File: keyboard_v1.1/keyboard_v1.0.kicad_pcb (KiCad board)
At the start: 2 copper layers, 100 x 100 mm, 138 parts, among them M3 MountingHole_3.2mm_M3, P1 USB_C_Plug, Q1 AO3400A, Q2 AO3400A, Q3 AO3400A, Q4 AO3400A, SW1 Cherry_MX_1u, SW10 Cherry_MX_1u, SW11 Cherry_MX_1u, SW12 Cherry_MX_1u, SW13 MTS-102, SW14 SW_DIP_x01, SW15 SW_DIP_x01, SW16 SW_DIP_x01, SW17 SW_DIP_x01, SW2 Cherry_MX_1u, SW3 Cherry_MX_1u, SW4 Cherry_MX_1u, SW5 Cherry_MX_1u, SW6 Cherry_MX_1u, SW7 Cherry_MX_1u, SW8 Cherry_MX_1u, SW9 Cherry_MX_1u, U1 max1737eei+T, U2 max1771esa+T, U3 max1771esa+T

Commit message: PCB layout done - 2022.07.25.
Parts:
- removed C25, C32, C33, C34, C35, C36, C37, C41, C46: 0.1uF, Capacitor_SMD:C_0805_2012Metric_Pad1.18x1.45mm_HandSolder
- removed C26: 47nF, Capacitor_SMD:C_0805_2012Metric_Pad1.18x1.45mm_HandSolder
- removed C27, C29, C30: 1nF, Capacitor_SMD:C_0805_2012Metric_Pad1.18x1.45mm_HandSolder
- removed C28: 4.7u, Capacitor_SMD:C_0805_2012Metric_Pad1.18x1.45mm_HandSolder
- removed C38, C39: 22pF, Capacitor_SMD:C_0805_2012Metric_Pad1.18x1.45mm_HandSolder
- removed C40: 68uF, Capacitor_THT:CP_Radial_D6.3mm_P2.50mm
- removed C42, C47: 2.2uF, Capacitor_SMD:C_0805_2012Metric_Pad1.18x1.45mm_HandSolder
- removed C43, C48: 47pF, Capacitor_SMD:C_0805_2012Metric_Pad1.18x1.45mm_HandSolder
- removed C44, C49: 47uF, Capacitor_THT:CP_Radial_D4.0mm_P1.50mm
- removed C45, C50: 22uF, Capacitor_SMD:C_0805_2012Metric_Pad1.18x1.45mm_HandSolder
- removed D35, D39: US1M, Diode_SMD:D_SMA
- removed D38: LED, LED_SMD:LED_0603_1608Metric_Pad1.05x0.95mm_HandSolder
- removed D40, D41, D42, D43: 1N5819, Diode_THT:D_DO-41_SOD81_P10.16mm_Horizontal
- removed L4, L5: 20uH, inductors:inductors
- removed the M3 at (135.0, 125.0)
- removed the M3 at (45.0, 125.0)
- removed the M3 at (135.0, 35.0)
- removed the M3 at (45.0, 35.0)
- removed Q1 (x2), Q2 (x2), Q3, Q4: AO3400A, Package_TO_SOT_SMD:SOT-23
- removed R30: 200K, Resistor_SMD:R_0805_2012Metric_Pad1.20x1.40mm_HandSolder
- removed R31: 470K, Resistor_SMD:R_0805_2012Metric_Pad1.20x1.40mm_HandSolder
- removed R32, R35: 0.1, Resistor_SMD:R_0805_2012Metric_Pad1.20x1.40mm_HandSolder
- removed R33: 100K, Resistor_SMD:R_0805_2012Metric_Pad1.20x1.40mm_HandSolder
- removed R34: 20K, Resistor_SMD:R_0805_2012Metric_Pad1.20x1.40mm_HandSolder
- removed SW14, SW15, SW16, SW17: SW_DIP_x01, Connector_PinHeader_2.54mm:PinHeader_1x02_P2.54mm_Vertical
- removed TH1: Thermistor_NTC, Capacitor_THT:C_Disc_D5.0mm_W2.5mm_P5.00mm
- removed U2, U3: max1771esa+T, max1771:max1771esa&plus_T
- added C13: 10uF, Capacitor_SMD:C_0805_2012Metric_Pad1.18x1.45mm_HandSolder, F.Cu at (80.8, 50.3)
- added C15: 22uF, Capacitor_SMD:C_0805_2012Metric_Pad1.18x1.45mm_HandSolder, F.Cu at (75.9, 54.2)
- added C16: 1uF, Capacitor_SMD:C_0805_2012Metric_Pad1.18x1.45mm_HandSolder, F.Cu at (77.9, 54.2)
- added C17: 22uF, Capacitor_SMD:C_0805_2012Metric_Pad1.18x1.45mm_HandSolder, F.Cu at (104.8, 53.2)
- added C18: 2.2uF, Capacitor_SMD:C_0805_2012Metric_Pad1.18x1.45mm_HandSolder, F.Cu at (112.8, 51.4)
- added C9: 4.7uF, Capacitor_SMD:C_0805_2012Metric_Pad1.18x1.45mm_HandSolder, F.Cu at (97.0, 32.9)
- added D14: FUXINSEMI DSK34 (SOD-123), Diode_SMD:D_SOD-123, F.Cu at (114.1, 47.2)
- added IC1: LN4056-ESOP8, SamacSys_Parts:SOIC127P600X175-9N, F.Cu at (98.8, 36.7)
- added JP1: Jumper_3_Bridged12, Connector_PinHeader_2.54mm:PinHeader_1x03_P2.54mm_Horizontal, F.Cu at (135.1, 71.7)
- added JP2: Jumper_3_Bridged12, Connector_PinHeader_2.54mm:PinHeader_1x03_P2.54mm_Horizontal, F.Cu at (135.1, 80.3)
- added JP3: Jumper_3_Bridged12, Connector_PinHeader_2.54mm:PinHeader_1x03_P2.54mm_Horizontal, F.Cu at (135.1, 97.8)
- added JP4: Jumper_3_Bridged12, Connector_PinHeader_2.54mm:PinHeader_1x03_P2.54mm_Horizontal, F.Cu at (135.2, 89.0)
- added M3: MountingHole_3.2mm_M3, MountingHole:MountingHole_3.2mm_M3, F.Cu at (135.4, 125.5)
- added M3: MountingHole_3.2mm_M3, MountingHole:MountingHole_3.2mm_M3, F.Cu at (135.9, 33.9)
- added M3: MountingHole_3.2mm_M3, MountingHole:MountingHole_3.2mm_M3, F.Cu at (44.3, 125.4)
- added M3: MountingHole_3.2mm_M3, MountingHole:MountingHole_3.2mm_M3, F.Cu at (44.6, 34.6)
- added PS1: HX3608, SamacSys_Parts:SOT95P280X125-6N, F.Cu at (81.0, 53.2)
- added R14: 10k, Resistor_SMD:R_0805_2012Metric_Pad1.20x1.40mm_HandSolder, F.Cu at (103.8, 39.6)
- added R15: 22k, Resistor_SMD:R_0805_2012Metric_Pad1.20x1.40mm_HandSolder, F.Cu at (71.5, 54.1)
- added R16: 3k, Resistor_SMD:R_0805_2012Metric_Pad1.20x1.40mm_HandSolder, F.Cu at (71.5, 57.8)
- added R17: 100K, Resistor_SMD:R_0805_2012Metric_Pad1.20x1.40mm_HandSolder, F.Cu at (105.8, 50.4)
- added R18: 9.1k, Resistor_SMD:R_0805_2012Metric_Pad1.20x1.40mm_HandSolder, F.Cu at (109.9, 46.7)
- added R19: 5.6k, Resistor_SMD:R_0805_2012Metric_Pad1.20x1.40mm_HandSolder, F.Cu at (105.1, 47.5)
- added TP2: TestPoint, TestPoint:TestPoint_Keystone_5010-5014_Multipurpose, F.Cu at (109.6, 39.4)
- BT1: footprint Connector_PinSocket_2.54mm:PinSocket_1x02_P2.54mm_Vertical -> Connector_PinSocket_2.54mm:PinSocket_1x02_P2.54mm_Horizontal
- C22: value 4.7u -> 2.2nF
- C23: value 47nF -> 10uF
- C24: value 0.1uF -> ?uF
- C31: value 0.1uF -> 4.7uF
- D13: value US1M -> FUXINSEMI DSK34 (SOD-123); footprint Diode_SMD:D_SMA -> Diode_SMD:D_SOD-123
- D36: value LED -> GREEN LED; footprint LED_SMD:LED_0603_1608Metric_Pad1.05x0.95mm_HandSolder -> LED_SMD:LED_0805_2012Metric_Pad1.15x1.40mm_HandSolder
- D37: value LED -> RED LED; footprint LED_SMD:LED_0603_1608Metric_Pad1.05x0.95mm_HandSolder -> LED_SMD:LED_0805_2012Metric_Pad1.15x1.40mm_HandSolder
- L1: value 22uH -> 3.3uH; footprint inductors:inductors -> inductors:inductor_koherelec
- L2, L3: value 20uH -> 6.8uH; footprint inductors:inductors -> inductors:inductor_koherelec
- R1, R2, R3: moved to F.Cu
- R10: value 1k -> 3k
- R12: value 0.1prec -> 10k; footprint Resistor_SMD:R_2512_6332Metric_Pad1.40x3.35mm_HandSolder -> Resistor_SMD:R_0805_2012Metric_Pad1.20x1.40mm_HandSolder
- R13: value 0.18prec -> 10k; footprint Resistor_THT:R_Axial_DIN0309_L9.0mm_D3.2mm_P25.40mm_Horizontal -> Resistor_SMD:R_0805_2012Metric_Pad1.20x1.40mm_HandSolder
- R9: value 1k -> 10K
- SW13: value MTS-102 -> SW_DPDT; footprint Switch_ApemInc:Apem_Inc.-25336NA-MFG -> Connector_PinHeader_2.54mm:PinHeader_1x03_P2.54mm_Horizontal
- U1: value max1737eei+T -> LMR62421XMF; footprint max1737:max1737eei&plus_T -> Package_TO_SOT_SMD:SOT-23-5
- moved C19 98.9 mm to (138.0, 39.4), turned to 0 degrees
- moved C20 98.4 mm to (138.0, 41.4), turned to 0 degrees
- moved C21 92.6 mm to (135.0, 40.6), turned to 90 degrees
- moved R5 89.4 mm to (131.6, 37.3), turned to -90 degrees
- moved R3 88.3 mm to (130.4, 111.3), turned to -90 degrees
- moved ESP32 87.0 mm to (133.4, 53.5), turned to -90 degrees
- moved R8 85.2 mm to (132.0, 103.9), turned to 90 degrees
- moved R2 83.9 mm to (128.5, 91.4), turned to -90 degrees
- moved R7 75.7 mm to (132.3, 86.4), turned to 90 degrees
- moved C12 74.5 mm to (52.0, 119.9), turned to 180 degrees
- moved C11 72.7 mm to (53.9, 79.7), turned to 180 degrees
- moved R9 72.3 mm to (132.3, 95.1)
- moved R6 70.1 mm to (132.3, 77.7), turned to 90 degrees
- moved C14 67.7 mm to (59.0, 108.7), turned to 0 degrees
- moved P1 67.3 mm to (122.8, 35.7), turned to 0 degrees
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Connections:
- C22 pad 1: Net-(C22-Pad1) -> 3.3V_OUT
- C22 pad 2: GND -> Net-(C22-Pad2)
- C23 pad 1: Net-(C23-Pad1) -> 3.3V_OUT
- C24 pad 1: Net-(C24-Pad1) -> 3.3V_OUT
- C31 pad 1: Net-(C31-Pad1) -> USB_Input_supply
- D13 pad 1: Net-(C36-Pad1) -> 5V_OUT
- D13 pad 2: USB_Input_supply -> Net-(D13-Pad2)
- D37 pad 2: Net-(D37-Pad2) -> Net-(D36-Pad2)
- ESP32 pad 4: 1st_Column -> 4th_Column
- ESP32 pad 5: 2nd_Column -> 3rd_Column
- ESP32 pad 6: 3rd_Column -> 2nd_Column
- ESP32 pad 7: 4th_Column -> 1st_Column
- L1 pad 1: Net-(C33-Pad2) -> SYSTEM_LOAD
- L1 pad 2: Net-(C34-Pad1) -> Net-(D13-Pad2)
- L2 pad 2: Net-(C44-Pad1) -> Net-(C18-Pad1)
- R10 pad 1: Net-(C31-Pad1) -> USB_Input_supply
- R10 pad 2: Net-(D37-Pad2) -> Net-(D36-Pad2)
- R11 pad 1: Net-(C31-Pad1) -> Net-(IC1-Pad2)
- R11 pad 2: Net-(D36-Pad2) -> GND
- R12 pad 1: Net-(C36-Pad1) -> USB_Input_supply
- R12 pad 2: SYSTEM_LOAD -> Net-(IC1-Pad8)
- R13 pad 1: Net-(C34-Pad1) -> USB_Input_supply
- R13 pad 2: Net-(C32-Pad1) -> /battery_charger/TEMP
- R6 pad 1: Net-(C27-Pad1) -> GND
- R6 pad 2: Net-(C24-Pad1) -> Net-(JP1-Pad3)
- R7 pad 1: Net-(C28-Pad1) -> GND
- R7 pad 2: Net-(R7-Pad2) -> Net-(JP2-Pad3)
- R8 pad 1: Net-(R7-Pad2) -> GND
- R8 pad 2: GND -> Net-(JP3-Pad3)
- R9 pad 1: Net-(C31-Pad1) -> GND
- SW13 pad 1: Net-(BT1-Pad1) -> SYSTEM_LOAD
- SW13 pad 2: unconnected-(SW13-Pad2) -> Net-(BT1-Pad1)
- SW13 pad 3: Net-(C32-Pad1) -> unconnected-(SW13-Pad3)
- U1 pad 1: Net-(C22-Pad1) -> Net-(C18-Pad1)
- U1 pad 2: Net-(C28-Pad1) -> GND
- U1 pad 3: Net-(C28-Pad1) -> Net-(C22-Pad2)
- U1 pad 5: Net-(C28-Pad1) -> SYSTEM_LOAD
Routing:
- net GND: track 710.0 -> 56.6 mm, vias 306 -> 357
- net 1st_Column: track 59.6 -> 138.7 mm, vias 5 -> 1
- net Net-(C48-Pad1): track 71.9 -> 0.00 mm, vias 2 -> 0
- net 5V_OUT: track 367.6 -> 304.5 mm, vias 17 -> 16
- net Net-(C49-Pad1): track 58.8 -> 0.00 mm
- net Net-(ESP32-Pad26): track 3.22 -> 60.1 mm, vias 0 -> 1
- net Net-(C32-Pad1): track 53.4 -> 0.00 mm, vias 3 -> 0
- net Net-(C18-Pad2): track 53.9 -> 7.44 mm
- net 2nd_Column: track 78.8 -> 118.6 mm, vias 3 -> 1
- net Net-(C34-Pad1): track 39.5 -> 0.00 mm, vias 2 -> 0
- net Net-(D38-Pad1): track 31.1 -> 0.00 mm, vias 2 -> 0
- net Net-(ESP32-Pad27): track 8.91 -> 39.2 mm, vias 0 -> 1
- net 3.3V_OUT: track 73.8 -> 103.6 mm, vias 0 -> 2
- net Net-(C44-Pad1): track 28.5 -> 0.00 mm, vias 1 -> 0
- net Net-(C33-Pad2): track 25.9 -> 0.00 mm
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
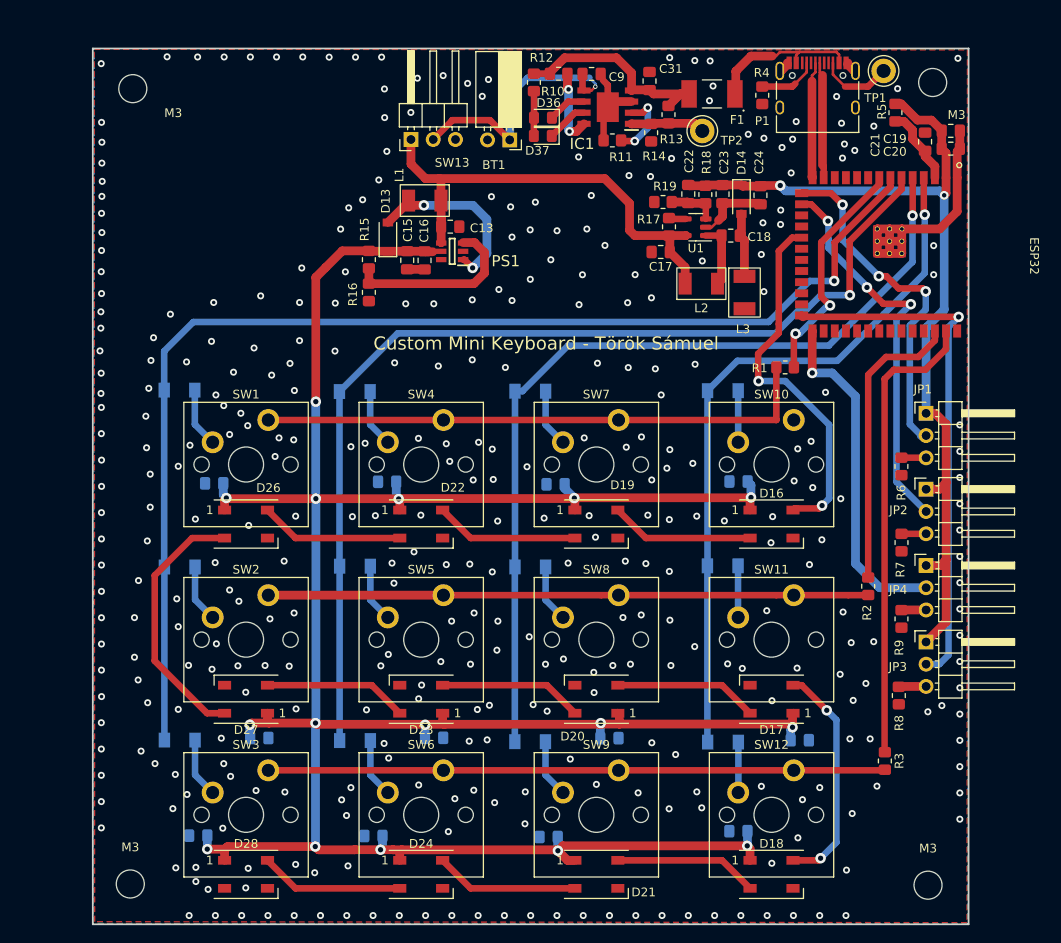
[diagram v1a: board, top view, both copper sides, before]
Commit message: Corrections on PCB design - 2022.08.04.
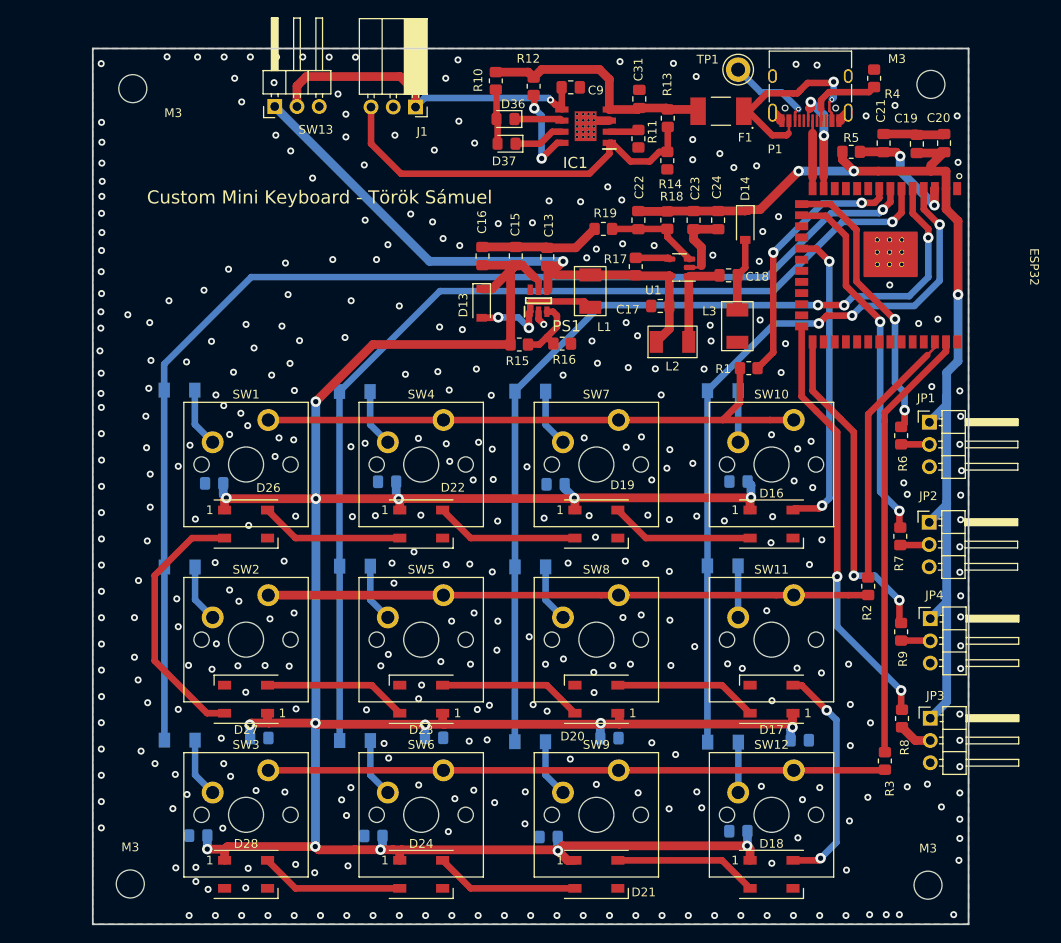
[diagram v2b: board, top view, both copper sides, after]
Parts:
- removed BT1: Battery_Cell, Connector_PinSocket_2.54mm:PinSocket_1x02_P2.54mm_Horizontal
- removed TP2: TestPoint, TestPoint:TestPoint_Keystone_5010-5014_Multipurpose
- added J1: Battery, TEMP, Connector_PinSocket_2.54mm:PinSocket_1x03_P2.54mm_Horizontal, F.Cu at (76.8, 36.7)
- moved R16 22.8 mm to (93.6, 63.7), turned to 0 degrees
- moved L1 21.5 mm to (96.8, 57.7), turned to 0 degrees
- moved R15 19.7 mm to (88.7, 63.8), turned to 0 degrees
- moved TP1 16.6 mm to (113.7, 32.4)
- moved SW13 16.0 mm to (60.8, 36.6)
- moved D13 13.1 mm to (84.4, 59.1), turned to -90 degrees
- moved R4 12.9 mm to (129.2, 33.4), turned to 90 degrees
- moved C15 12.4 mm to (88.3, 53.7), turned to 90 degrees
- moved C13 11.6 mm to (91.9, 53.8), turned to 90 degrees
- moved PS1 11.4 mm to (90.9, 58.8), turned to 90 degrees
- moved JP3 8.73 mm to (135.6, 106.5)
- moved R19 7.47 mm to (98.3, 50.6)
- moved L2 7.42 mm to (106.2, 63.5)
- moved R5 6.75 mm to (126.6, 41.8), turned to 0 degrees
- moved C16 6.64 mm to (84.5, 53.7), turned to 90 degrees
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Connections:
- JP1 pad 2: Net-(ESP32-Pad15) -> Net-(JP1-Pad2)
- JP1 pad 3: Net-(JP1-Pad3) -> GND
- JP2 pad 2: Net-(ESP32-Pad16) -> Net-(JP2-Pad2)
- JP2 pad 3: Net-(JP2-Pad3) -> GND
- JP3 pad 2: Net-(ESP32-Pad26) -> Net-(JP3-Pad2)
- JP3 pad 3: Net-(JP3-Pad3) -> GND
- JP4 pad 2: Net-(ESP32-Pad27) -> Net-(JP4-Pad2)
- JP4 pad 3: Net-(R9-Pad2) -> GND
- R6 pad 1: GND -> Net-(ESP32-Pad15)
- R6 pad 2: Net-(JP1-Pad3) -> Net-(JP1-Pad2)
- R7 pad 1: GND -> Net-(JP2-Pad2)
- R7 pad 2: Net-(JP2-Pad3) -> Net-(ESP32-Pad16)
- R8 pad 1: GND -> Net-(ESP32-Pad26)
- R8 pad 2: Net-(JP3-Pad3) -> Net-(JP3-Pad2)
- R9 pad 1: GND -> Net-(JP4-Pad2)
- R9 pad 2: Net-(R9-Pad2) -> Net-(ESP32-Pad27)
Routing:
- net /battery_charger/TEMP: track 8.47 -> 45.8 mm
- net GND: track 56.6 -> 36.9 mm, vias 357 -> 389
- net 5V_OUT: track 304.5 -> 322.0 mm
- net 3.3V_OUT: track 103.6 -> 120.6 mm, vias 2 -> 3
- net SYSTEM_LOAD: track 54.0 -> 67.6 mm, vias 0 -> 1
- net /DC-DC_Converters_5V/FB: track 20.7 -> 7.83 mm
- net Net-(ESP32-Pad26): track 60.1 -> 48.5 mm, vias 1 -> 2
- net Net-(C9-Pad1): track 30.3 -> 38.8 mm
- net Net-(ESP32-Pad15): track 39.5 -> 32.5 mm, vias 3 -> 2
- net LEDS: track 42.3 -> 35.5 mm
- net Net-(F1-Pad1): track 17.7 -> 24.2 mm, vias 0 -> 2
- net USB_D+: track 13.3 -> 7.76 mm
- net Net-(C22-Pad2): track 5.69 -> 10.8 mm
- net Net-(C21-Pad1): track 8.91 -> 13.9 mm, vias 0 -> 2
- net Net-(D13-Pad2): track 21.0 -> 16.1 mm
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
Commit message: Fixing unconnected tracks - 2022.08.09.
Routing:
- net GND: track 36.9 -> 73.7 mm, vias 389 -> 392
